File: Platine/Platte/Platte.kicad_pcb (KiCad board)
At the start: 2 copper layers, 31.1 x 31.1 mm, 21 parts, among them J1 Conn_01x07_MountingPin, J2 Conn_01x04_Socket, J3 Conn_01x04_Socket

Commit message: nicht so viel
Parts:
- moved C9 24.8 mm to (100.6, 73.3), turned to 90 degrees
- moved C8 23.6 mm to (99.6, 70.0), turned to -90 degrees
- moved R6 20.5 mm to (99.0, 75.1), turned to 90 degrees
- moved R5 18.3 mm to (97.8, 69.9), turned to 90 degrees
- moved C1 1.11 mm to (89.0, 74.2), turned to 0 degrees
- moved R3 1.02 mm to (89.4, 76.7)
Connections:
- C7 pad 1: Net-(C7-Pad1) -> /fil_da1
- C8 pad 1: Net-(C8-Pad1) -> /fil_da2
- C9 pad 1: Net-(C9-Pad1) -> /fil_da3
- J1 pad 3: /amp_data1 -> /fil_da1
- J1 pad 4: /amp_data2 -> /fil_da2
- J1 pad 5: /amp_data3 -> /fil_da3
- R4 pad 2: Net-(C7-Pad1) -> /fil_da1
- R5 pad 2: Net-(C8-Pad1) -> /fil_da2
- R6 pad 2: Net-(C9-Pad1) -> /fil_da3
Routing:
- net /amp_data3: track 11.5 -> 2.29 mm
- net +3.3VA: track 40.9 -> 47.9 mm
- net /fil_da1: track 0.00 -> 6.58 mm
- net /fil_da3: track 0.00 -> 6.31 mm
- net /amp_data2: track 8.41 -> 2.46 mm
- net /fil_da2: track 0.00 -> 5.86 mm
- net /analog_inp_1: track 0.00 -> 5.52 mm, vias 0 -> 1
- net /analog_inp_3: track 0.00 -> 2.49 mm

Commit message: PCBs ready
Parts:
- removed C5, C6: 0.1uF, Capacitor_SMD:C_0603_1608Metric_Pad1.08x0.95mm_HandSolder
- moved C4 34.5 mm to (104.5, 60.5), turned to 180 degrees
- moved C3 16.6 mm to (92.9, 58.5)
- moved C2 15.8 mm to (87.6, 67.0)
- moved C9 0.27 mm to (100.8, 73.5)
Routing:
- net +3.3VD: track 32.2 -> 39.8 mm
- net +3.3VA: track 47.9 -> 53.4 mm
- net /analog_inp_2: track 0.16 -> 4.49 mm, vias 0 -> 1
- net GNDD: track 18.9 -> 23.0 mm, vias 1 -> 2
- net GNDA: track 14.7 -> 17.2 mm
- net /fil_da3: track 6.31 -> 8.17 mm
- net /analog_inp_3: track 2.49 -> 4.16 mm, vias 0 -> 1

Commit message: mit Robin geredet
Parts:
- moved C4 5.82 mm to (98.8, 61.7)
- moved C9 0.25 mm to (100.5, 73.5), turned to -90 degrees
- moved C8 0.22 mm to (99.4, 69.9)
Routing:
- net +3.3VD: track 39.8 -> 35.2 mm
- net +3.3VA: track 53.4 -> 55.4 mm

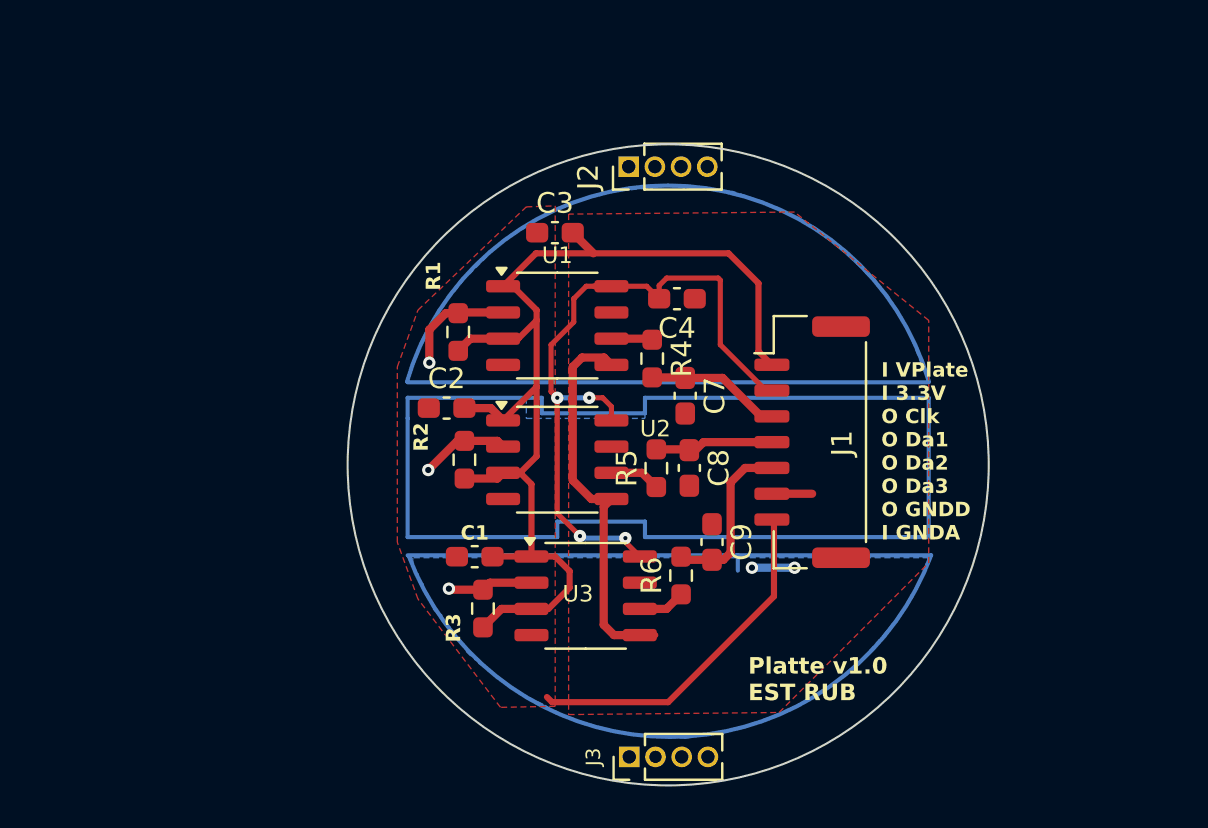
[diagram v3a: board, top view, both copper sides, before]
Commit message: Final circuits designed. Plate PCB ready, signal cond PCB still in process
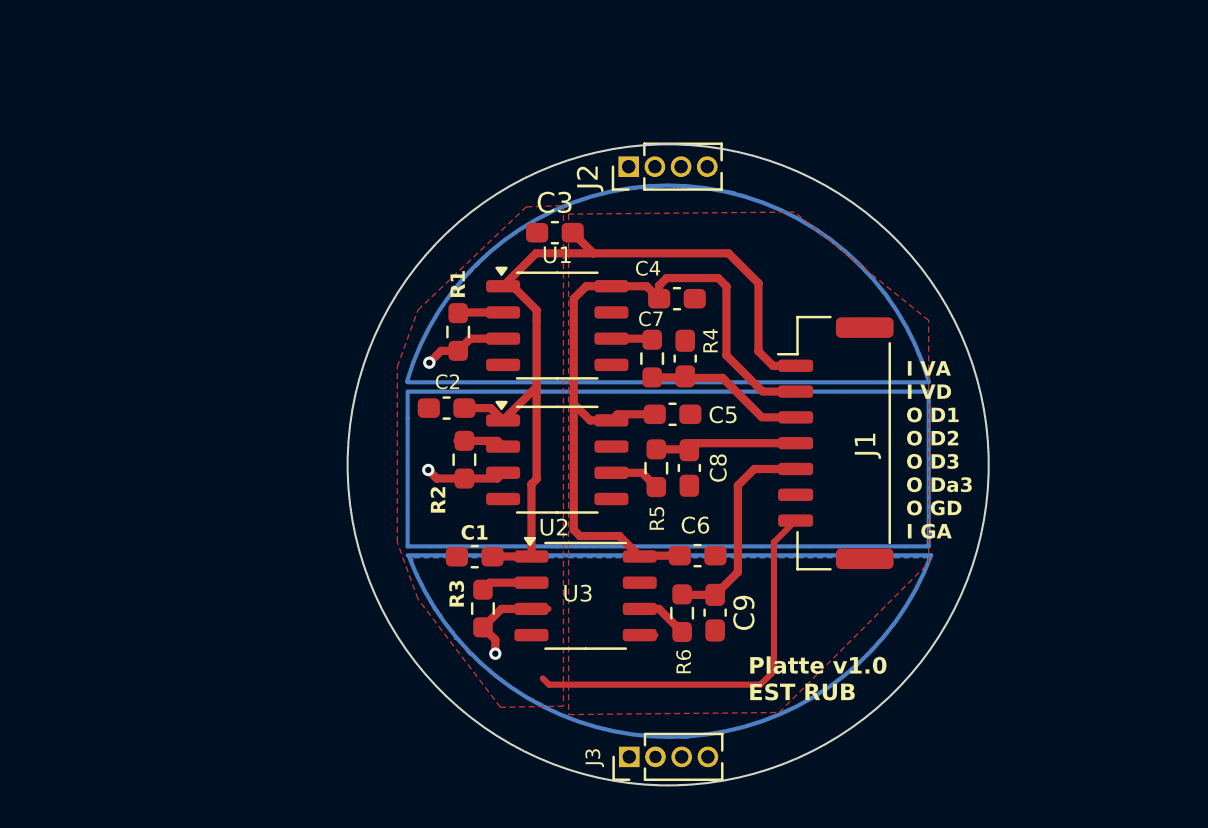
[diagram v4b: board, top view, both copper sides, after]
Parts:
- added C5: 0.1uF, Capacitor_SMD:C_0603_1608Metric_Pad1.08x0.95mm_HandSolder, F.Cu at (98.6, 67.3)
- added C6: 0.1uF, Capacitor_SMD:C_0603_1608Metric_Pad1.08x0.95mm_HandSolder, F.Cu at (99.8, 74.2)
- C7, C8, C9: value 5n -> 10n
- moved C9 3.43 mm to (100.7, 76.9)
- moved R6 1.83 mm to (99.0, 76.9)
- moved C7 1.80 mm to (99.2, 64.6), turned to 90 degrees
- moved J1 1.15 mm to (106.5, 68.7)
- turned R1 to -90 degrees
- turned R2 to -90 degrees
- turned R3 to -90 degrees
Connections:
- R1 pad 1: +3.3VA -> GNDA
- R2 pad 1: +3.3VA -> GNDA
- R3 pad 1: +3.3VA -> GNDA
- U1 pad 2: /analog_inp_1 -> GNDA
- U1 pad 3: +3.3VA -> /analog_inp_1
- U2 pad 2: /analog_inp_2 -> GNDA
- U2 pad 3: +3.3VA -> /analog_inp_2
- U3 pad 2: /analog_inp_3 -> GNDA
- U3 pad 3: +3.3VA -> /analog_inp_3
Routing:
- net GNDD: track 23.0 -> 1.02 mm, vias 2 -> 0
- net +3.3VA: track 55.4 -> 40.9 mm
- net GNDA: track 17.2 -> 26.8 mm
- net +3.3VD: track 35.2 -> 37.5 mm, vias 4 -> 0
- net /fil_da3: track 8.40 -> 10.5 mm
- net /analog_inp_1: track 5.52 -> 4.06 mm
- net /fil_da1: track 6.58 -> 7.68 mm
- net /fil_da2: track 5.86 -> 6.87 mm
- net /analog_inp_3: track 4.16 -> 5.07 mm
- net /analog_inp_2: track 4.49 -> 3.91 mm
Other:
- board text added: "I VA I VD O D1 O D2 O D3 O Da3 O GD I GA"
- board text removed: "I VPlate I 3.3V O Clk O Da1 O Da2 O Da3 O GNDD I GNDA"

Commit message: Made a few changes to PCBs and schematics
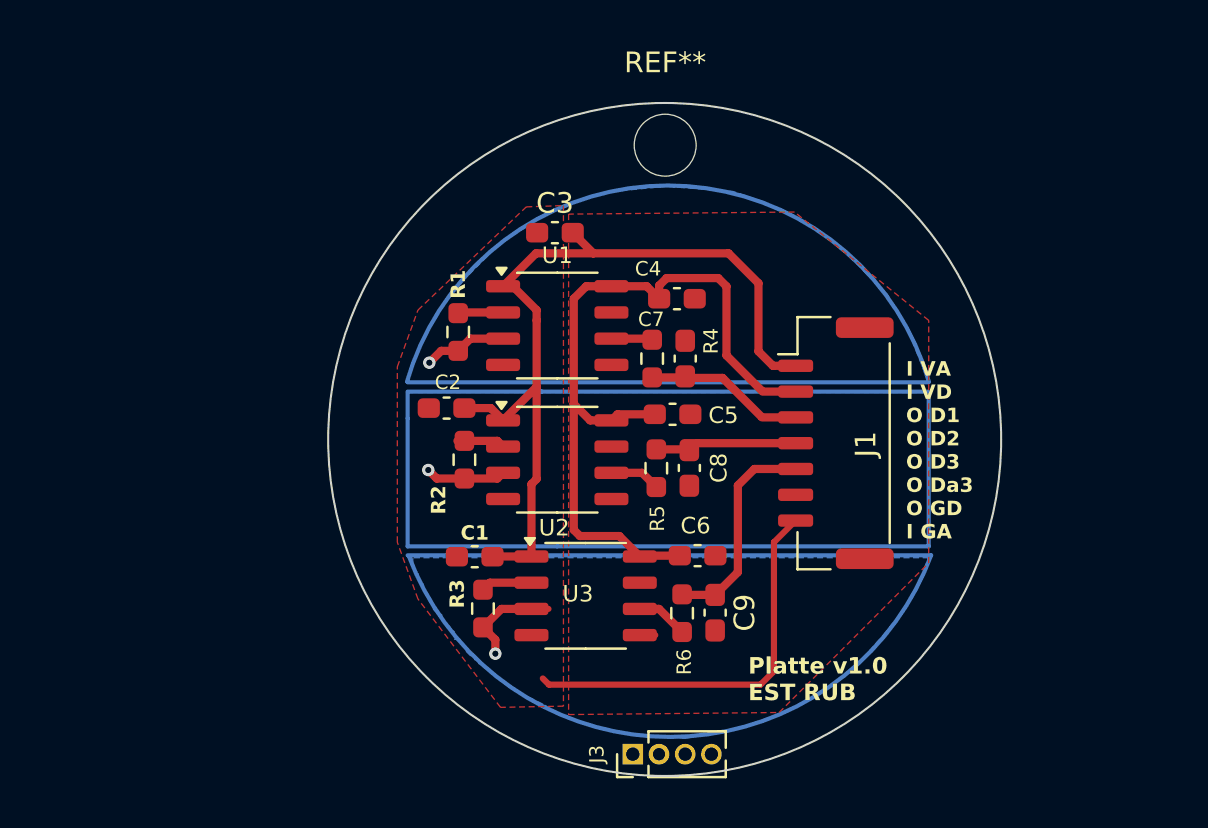
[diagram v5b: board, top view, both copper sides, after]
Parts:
- removed J2: Conn_01x04_Socket, Connector_PinHeader_1.27mm:PinHeader_1x04_P1.27mm_Vertical
- added REF**: MountingHole_3mm, MountingHole:MountingHole_3mm, F.Cu at (98.2, 54.3)
- moved J3 0.21 mm to (96.7, 83.8)
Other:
- board size 31.1 x 31.1 mm -> 32.6 x 32.6 mm

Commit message: Better shaping the Plates on the PCB
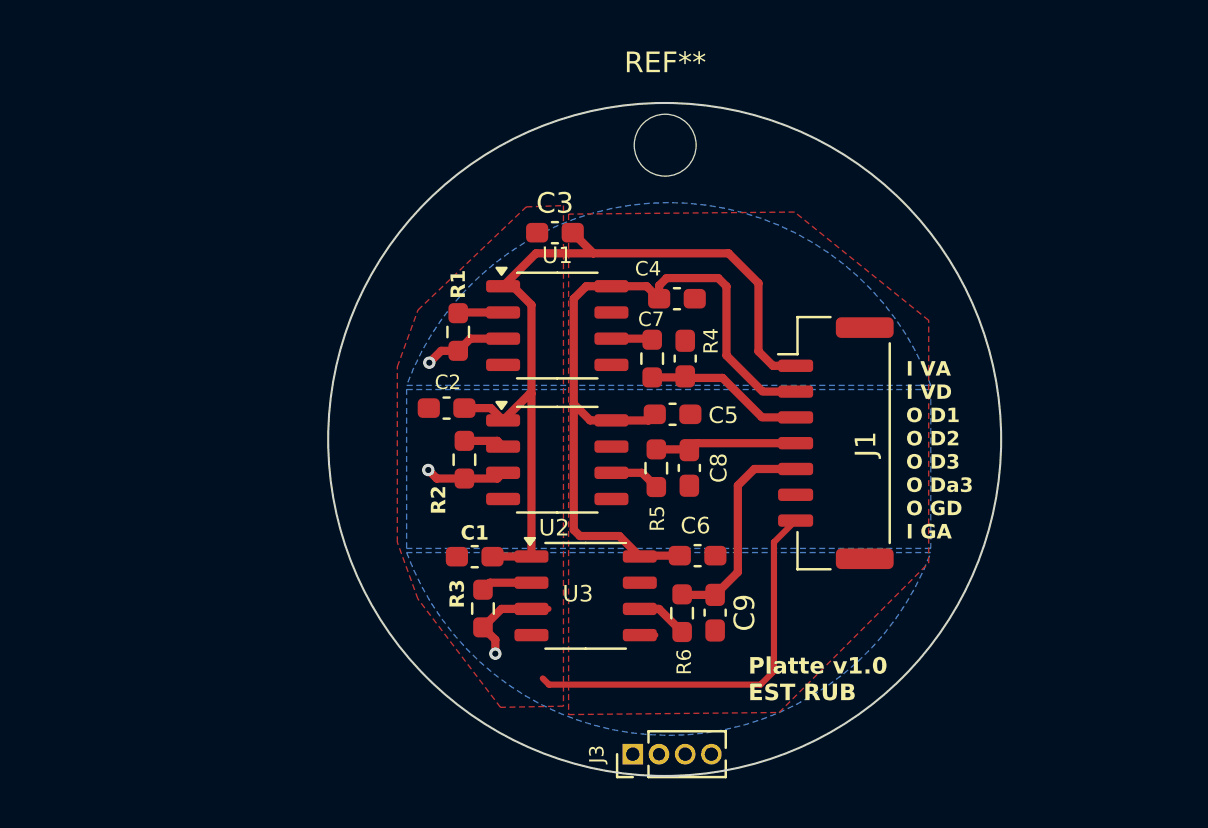
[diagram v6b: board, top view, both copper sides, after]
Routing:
- net +3.3VA: track 40.9 -> 40.3 mm

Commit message: All the changes until today
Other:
- board text added: "I VA I VD O D1 O D2 O D3 O GD I GA"
- board text removed: "I VA I VD O D1 O D2 O D3 O Da3 O GD I GA"
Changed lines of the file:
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@@
 		(layer "Edge.Cuts")
 	)
-	(gr_text "I VA\nI VD\nO D1\nO D2\nO D3\nO Da3\nO GD\nI GA"
+	(gr_text "I VA\nI VD\nO D1\nO D2\nO D3\nO GD\nI GA"
 		(at 109.9 73.4 0)
 		(layer "F.SilkS")
